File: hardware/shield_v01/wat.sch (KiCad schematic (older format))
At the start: 51 parts, among them P1 PINZA_1, P10 SCL-INT6, P102 CAUDAL_1, P103 V_IN, P106 18b20, P109 LCD_I2C, P11 SDA-INT5, P110 ARD_DI_06, P111 ARD_ALI_04, P2 PINZA_7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

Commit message: desrrollo pcb
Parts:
- renumbered R9 to R104, R104 to R9
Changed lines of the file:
@@
 $EndComp
 $Comp
-L R R104
+L R R9
 U 1 1 58A0503E
 P 10060 3405
-F 0 "R104" V 10140 3405 50  0000 C CNN
+F 0 "R9" V 10140 3405 50  0000 C CNN
 F 1 "2K" V 10060 3405 50  0000 C CNN
 F 2 "Resistors_ThroughHole:Resistor_Horizontal_RM10mm" V 9990 3405 50  0001 C CNN
@@
 $EndComp
 $Comp
-L R R9
+L R R104
 U 1 1 59AD5987
 P 7115 5830
-F 0 "R9" V 7195 5830 50  0000 C CNN
+F 0 "R104" V 7195 5830 50  0000 C CNN
 F 1 "R18" V 7115 5830 50  0000 C CNN
 F 2 "Resistors_ThroughHole:Resistor_Horizontal_RM10mm" V 7045 5830 50  0001 C CNN
@@
 Text Label 4310 6785 0    60   ~ 0
 Ref_medida
-Text Label 1035 4030 0    60   ~ 0
-Ves_3V3
 $Comp
 L CONN_01X04 P111
@@
 Text Label 5395 7235 0    60   ~ 0
 intensidad_8
+Text Label 1035 3970 0    60   ~ 0
+Vpc_5V
 $EndSCHEMATC

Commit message: desarrollo pcb v0
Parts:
- removed C102, C103: 100nF, Capacitors_ThroughHole:C_Disc_D3_P2.5, symbol C
- removed R104: R18, Resistors_ThroughHole:Resistor_Horizontal_RM10mm, symbol R
- added C1, C2: 100nF, Capacitors_ThroughHole:C_Disc_D3_P2.5, symbol C
- added R12: R18, Resistors_ThroughHole:Resistor_Horizontal_RM10mm, symbol R
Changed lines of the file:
@@
 $EndDescr
 $Comp
-L GND #PWR01
+L GND #PWR2
 U 1 1 584D06FF
 P 1190 1000
-F 0 "#PWR01" H 1190 750 50  0001 C CNN
+F 0 "#PWR2" H 1190 750 50  0001 C CNN
 F 1 "GND" H 1190 850 50  0000 C CNN
 F 2 "" H 1190 1000 50  0000 C CNN
@@
 $EndComp
 $Comp
-L PWR_FLAG #FLG02
+L PWR_FLAG #FLG1
 U 1 1 584D0E54
 P 1190 950
-F 0 "#FLG02" H 1190 1045 50  0001 C CNN
+F 0 "#FLG1" H 1190 1045 50  0001 C CNN
 F 1 "PWR_FLAG" H 1190 1130 50  0000 C CNN
 F 2 "" H 1190 950 50  0000 C CNN
@@
 $EndComp
 $Comp
-L GND #PWR03
+L GND #PWR11
 U 1 1 58501AA0
 P 10100 2550
-F 0 "#PWR03" H 10100 2300 50  0001 C CNN
+F 0 "#PWR11" H 10100 2300 50  0001 C CNN
 F 1 "GND" H 10100 2400 50  0000 C CNN
 F 2 "" H 10100 2550 50  0000 C CNN
@@
 $EndComp
 $Comp
-L PWR_FLAG #FLG04
+L PWR_FLAG #FLG2
 U 1 1 5857A9BC
 P 1690 950
-F 0 "#FLG04" H 1690 1045 50  0001 C CNN
+F 0 "#FLG2" H 1690 1045 50  0001 C CNN
 F 1 "PWR_FLAG" H 1690 1130 50  0000 C CNN
 F 2 "" H 1690 950 50  0000 C CNN
@@
 $EndComp
 $Comp
-L VCC #PWR05
+L VCC #PWR6
 U 1 1 5857A9F3
 P 1690 1100
-F 0 "#PWR05" H 1690 950 50  0001 C CNN
+F 0 "#PWR6" H 1690 950 50  0001 C CNN
 F 1 "VCC" H 1690 1250 50  0000 C CNN
 F 2 "" H 1690 1100 50  0000 C CNN
@@
 $EndComp
 $Comp
-L GND #PWR06
+L GND #PWR3
 U 1 1 5857C83E
 P 1265 2375
-F 0 "#PWR06" H 1265 2125 50  0001 C CNN
+F 0 "#PWR3" H 1265 2125 50  0001 C CNN
 F 1 "GND" H 1265 2225 50  0000 C CNN
 F 2 "" H 1265 2375 50  0000 C CNN
@@
 $EndComp
 $Comp
-L GND #PWR07
+L GND #PWR5
 U 1 1 5872416F
 P 1460 3515
-F 0 "#PWR07" H 1460 3265 50  0001 C CNN
+F 0 "#PWR5" H 1460 3265 50  0001 C CNN
 F 1 "GND" H 1460 3365 50  0000 C CNN
 F 2 "" H 1460 3515 50  0000 C CNN
@@
 $EndComp
 $Comp
-L GND #PWR08
+L GND #PWR12
 U 1 1 58A05050
 P 10160 3880
-F 0 "#PWR08" H 10160 3630 50  0001 C CNN
+F 0 "#PWR12" H 10160 3630 50  0001 C CNN
 F 1 "GND" H 10160 3730 50  0000 C CNN
 F 2 "" H 10160 3880 50  0000 C CNN
@@
 scl
 $Comp
-L GND #PWR09
+L GND #PWR10
 U 1 1 58A94056
 P 8725 1140
-F 0 "#PWR09" H 8725 890 50  0001 C CNN
+F 0 "#PWR10" H 8725 890 50  0001 C CNN
 F 1 "GND" H 8725 990 50  0000 C CNN
 F 2 "" H 8725 1140 50  0000 C CNN
@@
 18b20
 $Comp
-L GND #PWR010
+L GND #PWR8
 U 1 1 58A9B29F
 P 5580 3195
-F 0 "#PWR010" H 5580 2945 50  0001 C CNN
+F 0 "#PWR8" H 5580 2945 50  0001 C CNN
 F 1 "GND" H 5580 3045 50  0000 C CNN
 F 2 "" H 5580 3195 50  0000 C CNN
@@
 NoConn ~ 6755 1320
 $Comp
-L GND #PWR011
+L GND #PWR9
 U 1 1 58BE924F
 P 6905 1220
-F 0 "#PWR011" H 6905 970 50  0001 C CNN
+F 0 "#PWR9" H 6905 970 50  0001 C CNN
 F 1 "GND" H 6905 1070 50  0000 C CNN
 F 2 "" H 6905 1220 50  0000 C CNN
@@
 $EndComp
 $Comp
-L GND #PWR012
+L GND #PWR7
 U 1 1 58C1BA7B
 P 3855 4145
-F 0 "#PWR012" H 3855 3895 50  0001 C CNN
+F 0 "#PWR7" H 3855 3895 50  0001 C CNN
 F 1 "GND" H 3855 3995 50  0000 C CNN
 F 2 "" H 3855 4145 50  0000 C CNN
@@
 $EndComp
 $Comp
-L GND #PWR013
+L GND #PWR4
 U 1 1 59AD1454
 P 1360 5015
-F 0 "#PWR013" H 1360 4765 50  0001 C CNN
+F 0 "#PWR4" H 1360 4765 50  0001 C CNN
 F 1 "GND" H 1360 4865 50  0000 C CNN
 F 2 "" H 1360 5015 50  0000 C CNN
@@
 $EndComp
 $Comp
-L GND #PWR014
+L GND #PWR1
 U 1 1 59AD1455
 P 1035 5010
-F 0 "#PWR014" H 1035 4760 50  0001 C CNN
+F 0 "#PWR1" H 1035 4760 50  0001 C CNN
 F 1 "GND" H 1035 4860 50  0000 C CNN
 F 2 "" H 1035 5010 50  0000 C CNN
@@
 	1    0    0    -1
 $EndComp
-$Comp
-L C C102
-U 1 1 59AD219A
-P 2205 5840
-F 0 "C102" H 2230 5940 50  0000 L CNN
-F 1 "100nF" H 2230 5740 50  0000 L CNN
-F 2 "Capacitors_ThroughHole:C_Disc_D3_P2.5" H 2243 5690 50  0001 C CNN
-F 3 "" H 2205 5840 50  0000 C CNN
-	1    2205 5840
-	1    0    0    -1
-$EndComp
 Text Label 1555 4495 0    60   ~ 0
 Ref_medida
@@
 $EndComp
 $Comp
-L R R104
-U 1 1 59AD5987
-P 7115 5830
-F 0 "R104" V 7195 5830 50  0000 C CNN
-F 1 "R18" V 7115 5830 50  0000 C CNN
-F 2 "Resistors_ThroughHole:Resistor_Horizontal_RM10mm" V 7045 5830 50  0001 C CNN
-F 3 "" H 7115 5830 50  0000 C CNN
-	1    7115 5830
-	1    0    0    -1
-$EndComp
-$Comp
 L C C7
 U 1 1 59AD598D
@@
 F 3 "" H 2960 7005 50  0000 C CNN
 	1    2960 7005
-	1    0    0    -1
-$EndComp
-$Comp
-L C C103
-U 1 1 59AD623C
-P 3285 7005
-F 0 "C103" H 3310 7105 50  0000 L CNN
-F 1 "100nF" H 3310 6905 50  0000 L CNN
-F 2 "Capacitors_ThroughHole:C_Disc_D3_P2.5" H 3323 6855 50  0001 C CNN
-F 3 "" H 3285 7005 50  0000 C CNN
-	1    3285 7005
 	1    0    0    -1
 $EndComp
@@
 Text Label 1035 3970 0    60   ~ 0
 Vpc_5V
+$Comp
+L R R12
+U 1 1 59AFCC68
+P 7115 5830
+F 0 "R12" V 7195 5830 50  0000 C CNN
+F 1 "R18" V 7115 5830 50  0000 C CNN
+F 2 "Resistors_ThroughHole:Resistor_Horizontal_RM10mm" V 7045 5830 50  0001 C CNN
+F 3 "" H 7115 5830 50  0000 C CNN
+	1    7115 5830
+	1    0    0    -1
+$EndComp
+$Comp
+L C C1
+U 1 1 59AFE00D
+P 2205 5845
+F 0 "C1" H 2230 5945 50  0000 L CNN
+F 1 "100nF" H 2230 5745 50  0000 L CNN
+F 2 "Capacitors_ThroughHole:C_Disc_D3_P2.5" H 2243 5695 50  0001 C CNN
+F 3 "" H 2205 5845 50  0000 C CNN
+	1    2205 5845
+	1    0    0    -1
+$EndComp
+$Comp
+L C C2
+U 1 1 59AFE386
+P 3285 7005
+F 0 "C2" H 3310 7105 50  0000 L CNN
+F 1 "100nF" H 3310 6905 50  0000 L CNN
+F 2 "Capacitors_ThroughHole:C_Disc_D3_P2.5" H 3323 6855 50  0001 C CNN
+F 3 "" H 3285 7005 50  0000 C CNN
+	1    3285 7005
+	1    0    0    -1
+$EndComp
 $EndSCHEMATC

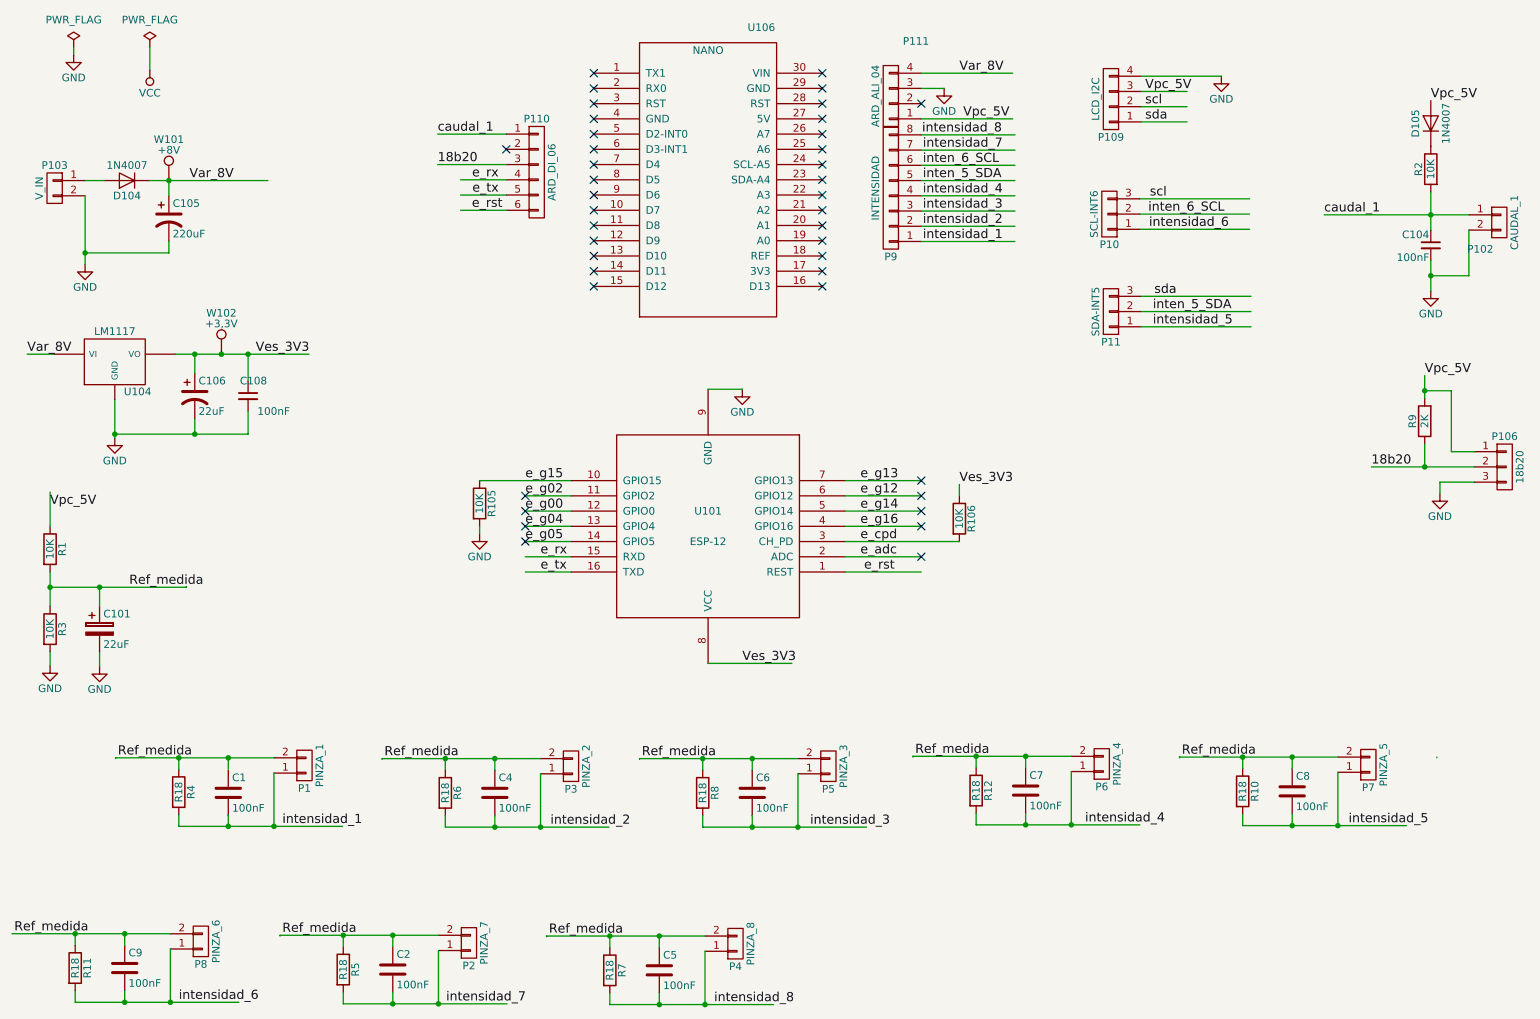
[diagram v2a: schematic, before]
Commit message: pcb simplificar a 6 medidas
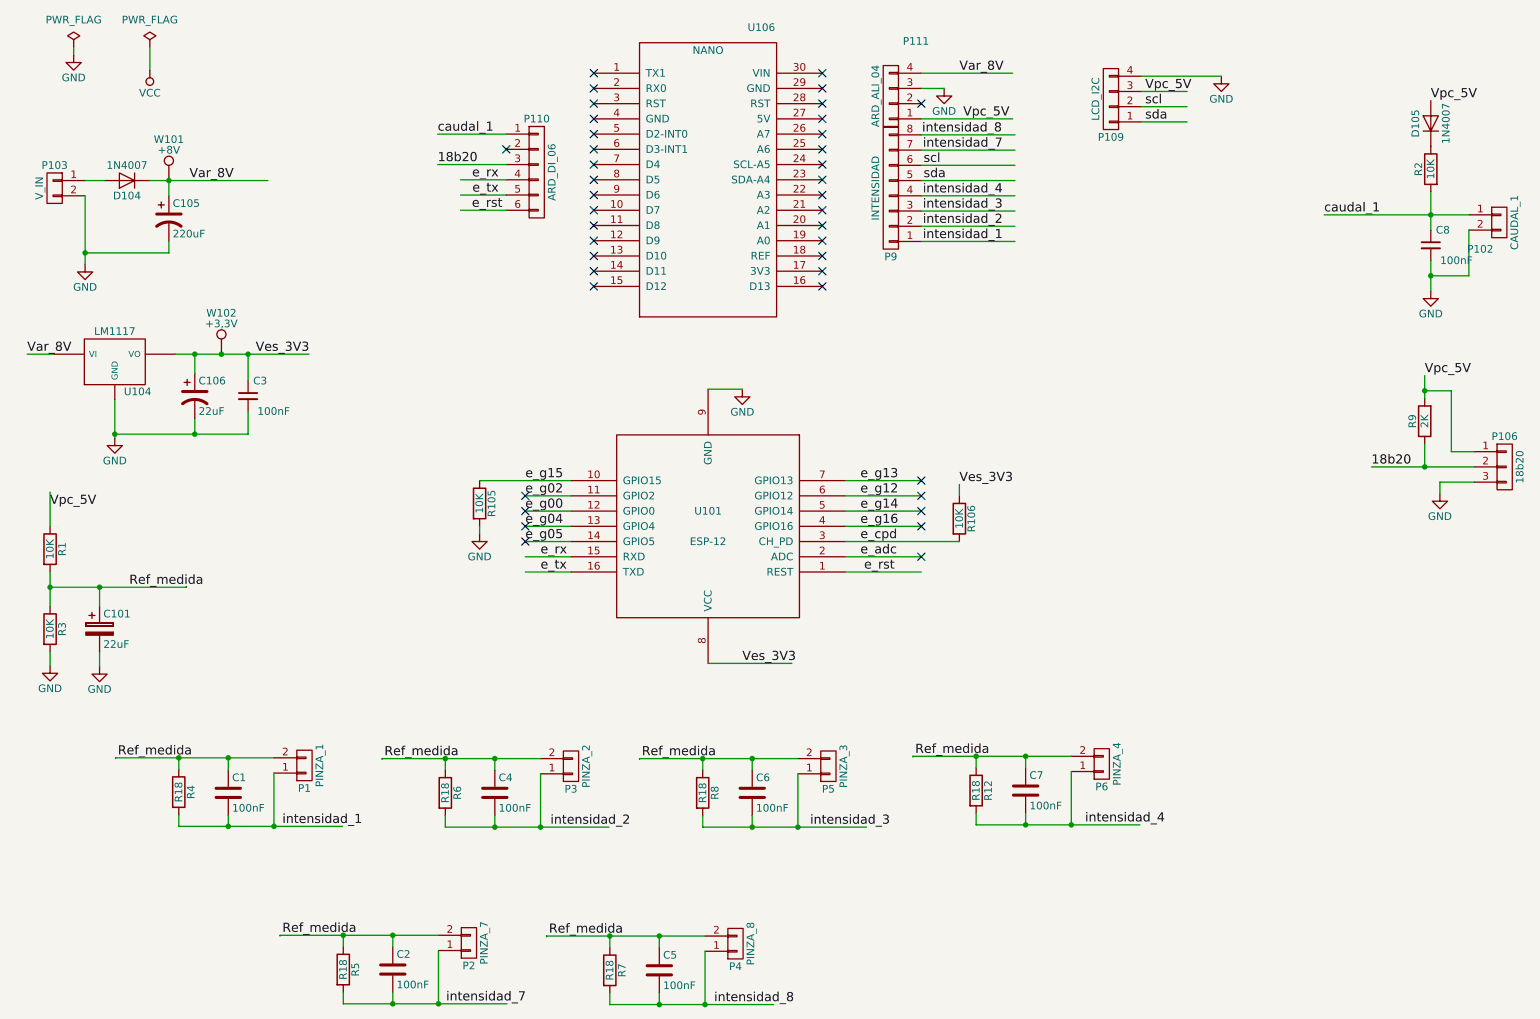
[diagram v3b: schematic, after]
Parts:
- removed C104, C108: 100nF, Capacitors_ThroughHole:C_Disc_D3_P2.5, symbol C_Small
- removed C8, C9: 100nF, Capacitors_ThroughHole:C_Disc_D3_P2.5, symbol C
- removed P10: SCL-INT6, Pin_Headers:Pin_Header_Straight_1x03, symbol CONN_01X03
- removed P11: SDA-INT5, Pin_Headers:Pin_Header_Straight_1x03, symbol CONN_01X03
- removed P7: PINZA_5, Connect:bornier2, symbol CONN_01X02
- removed P8: PINZA_6, Connect:bornier2, symbol CONN_01X02
- removed R10, R11: R18, Resistors_ThroughHole:Resistor_Horizontal_RM10mm, symbol R
- added C3, C8: 100nF, Capacitors_THT:C_Disc_D5.0mm_W2.5mm_P5.00mm, symbol C_Small
- C1, C2, C4, C5, C6, C7: footprint Capacitors_ThroughHole:C_Disc_D3_P2.5 -> Capacitors_THT:C_Disc_D5.0mm_W2.5mm_P5.00mm
- C101, C105, C106: footprint Capacitors_ThroughHole:C_Radial_D5_L11_P2 -> Capacitors_THT:CP_Radial_D5.0mm_P2.00mm
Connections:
- net labels removed: inten_5_SDA, inten_6_SCL, intensidad_5, intensidad_6
- wire segments 144 -> 122

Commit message: pcb cambio de valores de resistencias de carga
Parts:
- R12, R8: value R18 -> R20
- R4, R6: value R18 -> 10k
- R5, R7: value R18 -> R10
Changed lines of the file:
@@
 P 1880 5840
 F 0 "R4" V 1960 5840 50  0000 C CNN
-F 1 "R18" V 1880 5840 50  0000 C CNN
+F 1 "10k" V 1880 5840 50  0000 C CNN
 F 2 "Resistors_ThroughHole:Resistor_Horizontal_RM10mm" V 1810 5840 50  0001 C CNN
 F 3 "" H 1880 5840 50  0000 C CNN
@@
 P 3630 5845
 F 0 "R6" V 3710 5845 50  0000 C CNN
-F 1 "R18" V 3630 5845 50  0000 C CNN
+F 1 "10k" V 3630 5845 50  0000 C CNN
 F 2 "Resistors_ThroughHole:Resistor_Horizontal_RM10mm" V 3560 5845 50  0001 C CNN
 F 3 "" H 3630 5845 50  0000 C CNN
@@
 P 5320 5845
 F 0 "R8" V 5400 5845 50  0000 C CNN
-F 1 "R18" V 5320 5845 50  0000 C CNN
+F 1 "R20" V 5320 5845 50  0000 C CNN
 F 2 "Resistors_ThroughHole:Resistor_Horizontal_RM10mm" V 5250 5845 50  0001 C CNN
 F 3 "" H 5320 5845 50  0000 C CNN
@@
 P 2960 7005
 F 0 "R5" V 3040 7005 50  0000 C CNN
-F 1 "R18" V 2960 7005 50  0000 C CNN
+F 1 "R10" V 2960 7005 50  0000 C CNN
 F 2 "Resistors_ThroughHole:Resistor_Horizontal_RM10mm" V 2890 7005 50  0001 C CNN
 F 3 "" H 2960 7005 50  0000 C CNN
@@
 P 7115 5830
 F 0 "R12" V 7195 5830 50  0000 C CNN
-F 1 "R18" V 7115 5830 50  0000 C CNN
+F 1 "R20" V 7115 5830 50  0000 C CNN
 F 2 "Resistors_ThroughHole:Resistor_Horizontal_RM10mm" V 7045 5830 50  0001 C CNN
 F 3 "" H 7115 5830 50  0000 C CNN
@@
 P 4710 7010
 F 0 "R7" V 4790 7010 50  0000 C CNN
-F 1 "R18" V 4710 7010 50  0000 C CNN
+F 1 "R10" V 4710 7010 50  0000 C CNN
 F 2 "Resistors_ThroughHole:Resistor_Horizontal_RM10mm" V 4640 7010 50  0001 C CNN
 F 3 "" H 4710 7010 50  0000 C CNN
